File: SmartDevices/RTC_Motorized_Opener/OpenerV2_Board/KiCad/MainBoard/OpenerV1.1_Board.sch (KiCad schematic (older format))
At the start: 60 parts, among them IC1 CD4011BM96, J1 Motor, J2 Conn_01x02, J3 Conn_02x03_Odd_Even, J8 Conn_01x06, Q1 NPN, Q2 2N3904, Q3 AO3401A, Q4 AO3400A, Q5 2N3904, Q6 AO3400A, Q7 AO3401A, Q8 AO3400A, Q9 2N3904, SW1 Reset, SW2 Open, SW3 Menu, SW4 Close, U1 ATmega328P-AU, U2 MIC5205-5.0YM5, U3 DS1307, Y1 8/16MHz, Y2 32.768KHz

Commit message: Fixed TX RX Swapped pins
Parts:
- IC1: symbol Custom:CD4011BM96 -> OpenerV1.1_Board-rescue:CD4011BM96-Custom
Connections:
- net Tx0: now also J8.2 (Pin_2); no longer J8.3 (Pin_3)
- net at R20.1: now also J8.3 (Pin_3); no longer J8.2 (Pin_2)
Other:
- moved on the sheet: R20
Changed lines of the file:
@@
 Text Notes 3200 6700 0    50   ~ 0
 FTDI Header
+Text GLabel 3950 7450 2    50   Input ~ 0
+Tx0
 Text GLabel 3950 7350 2    50   Input ~ 0
-Tx0
-Text GLabel 3950 7450 2    50   Input ~ 0
 Rx0
 $Comp
@@
 $EndComp
 $Comp
-L Custom:CD4011BM96 IC1
+L OpenerV1.1_Board-rescue:CD4011BM96-Custom IC1
 U 1 1 5FB34D05
 P 9450 3500
@@
 L Device:R R20
 U 1 1 5FF1CF55
-P 3750 7450
-F 0 "R20" V 3957 7450 50  0000 C CNN
-F 1 "10K" V 3866 7450 50  0000 C CNN
-F 2 "Resistor_SMD:R_0805_2012Metric" V 3680 7450 50  0001 C CNN
-F 3 "~" H 3750 7450 50  0001 C CNN
-	1    3750 7450
-	0    -1   -1   0
-$EndComp
-Wire Wire Line
-	3600 7450 3550 7450
-Wire Wire Line
-	3900 7450 3950 7450
-Wire Wire Line
-	3550 7350 3950 7350
+P 3750 7350
+F 0 "R20" V 3957 7350 50  0000 C CNN
+F 1 "10K" V 3866 7350 50  0000 C CNN
+F 2 "Resistor_SMD:R_0805_2012Metric" V 3680 7350 50  0001 C CNN
+F 3 "~" H 3750 7350 50  0001 C CNN
+	1    3750 7350
+	0    -1   -1   0
+$EndComp
+Wire Wire Line
+	3600 7350 3550 7350
+Wire Wire Line
+	3900 7350 3950 7350
+Wire Wire Line
+	3550 7450 3950 7450
 Text GLabel 4100 3200 2    50   Input ~ 0
 DTR_FTDI

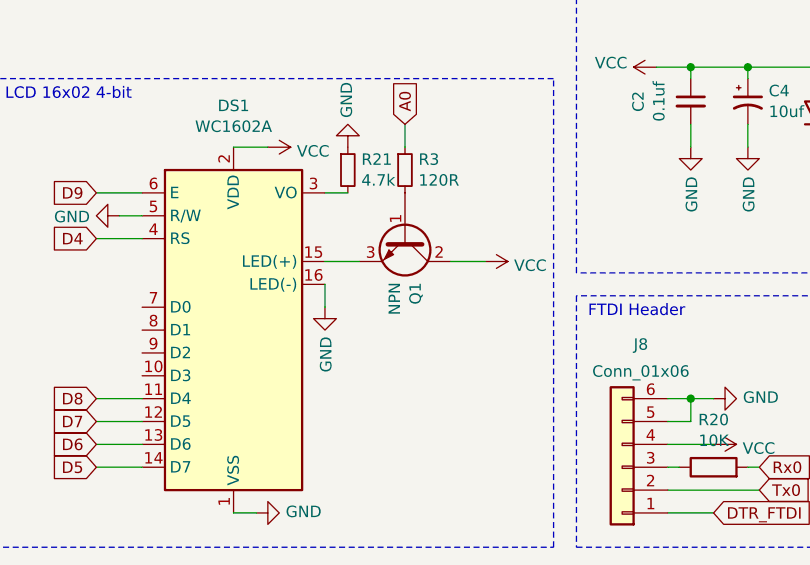
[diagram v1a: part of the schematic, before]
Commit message: Fixed Transistor Orientation
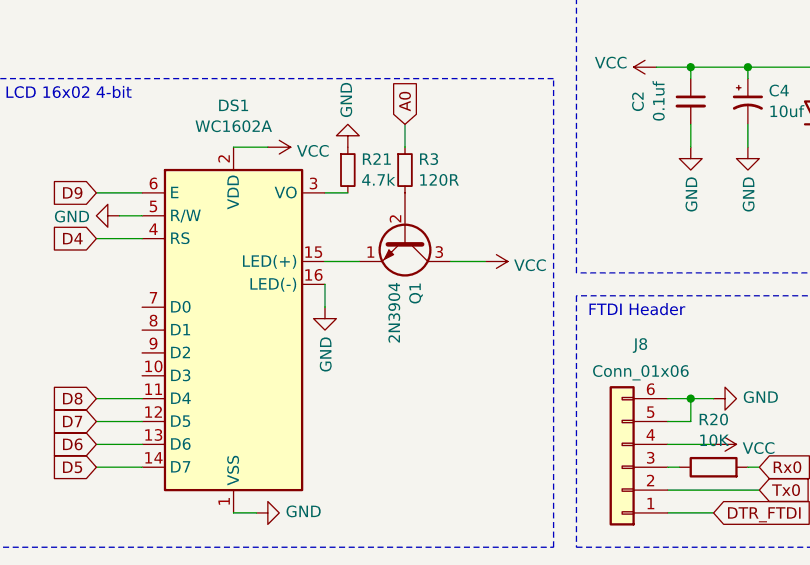
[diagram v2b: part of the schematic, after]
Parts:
- removed Q1: NPN, Package_TO_SOT_THT:TO-92, symbol Device:Q_NPN_BCE
- added Q1: 2N3904, Package_TO_SOT_THT:TO-92_Inline_Wide, symbol Transistor_BJT:2N3904
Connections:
- net VCC: now also Q1.3 (C)
- net at DS1.15 (LED(+)): now also Q1.1 (E)
- net at R3.2: now also Q1.2 (B)
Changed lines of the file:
@@
 	1    0    0    -1
-$EndComp
-$Comp
-L Device:Q_NPN_BCE Q1
-U 1 1 5EAD49E6
-P 2400 6350
-F 0 "Q1" H 2591 6396 50  0000 L CNN
-F 1 "NPN" H 2591 6305 50  0000 L CNN
-F 2 "Package_TO_SOT_THT:TO-92" H 2600 6450 50  0001 C CNN
-F 3 "~" H 2400 6350 50  0001 C CNN
-	1    2400 6350
-	0    1    1    0
 $EndComp
 Text GLabel 3050 3750 2    50   Input ~ 0
@@
 Wire Wire Line
 	2150 6150 2050 6150
+$Comp
+L Transistor_BJT:2N3904 Q1
+U 1 1 61F3A9A1
+P 2400 6350
+F 0 "Q1" H 2590 6396 50  0000 L CNN
+F 1 "2N3904" H 2590 6305 50  0000 L CNN
+F 2 "Package_TO_SOT_THT:TO-92_Inline_Wide" H 2600 6275 50  0001 L CIN
+F 3 "https://www.onsemi.com/pub/Collateral/2N3903-D.PDF" H 2400 6350 50  0001 L CNN
+	1    2400 6350
+	0    1    1    0
+$EndComp
 $EndSCHEMATC
